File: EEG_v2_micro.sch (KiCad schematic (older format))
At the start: 0 parts

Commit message: Added CC2540 Bluetooth chip to library
Also added CC2540 to sch
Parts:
- added U6: CC2540, symbol CC2540
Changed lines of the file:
@@
 Sheet 2 4
 Title "Project Synapse Prototype Board"
-Date "12 jan 2015"
+Date "13 jan 2015"
 Rev "A.b"
 Comp "Senior Design 14-15"
@@
 Comment4 ""
 $EndDescr
+$Comp
+L CC2540 U6
+U 1 1 54B4D13C
+P 5450 4250
+F 0 "U6" H 5450 4150 60  0000 C CNN
+F 1 "CC2540" H 5450 4300 60  0000 C CNN
+F 2 "" H 5450 4300 60  0000 C CNN
+F 3 "" H 5450 4300 60  0000 C CNN
+	1    5450 4250
+	1    0    0    -1
+$EndComp
 $EndSCHEMATC

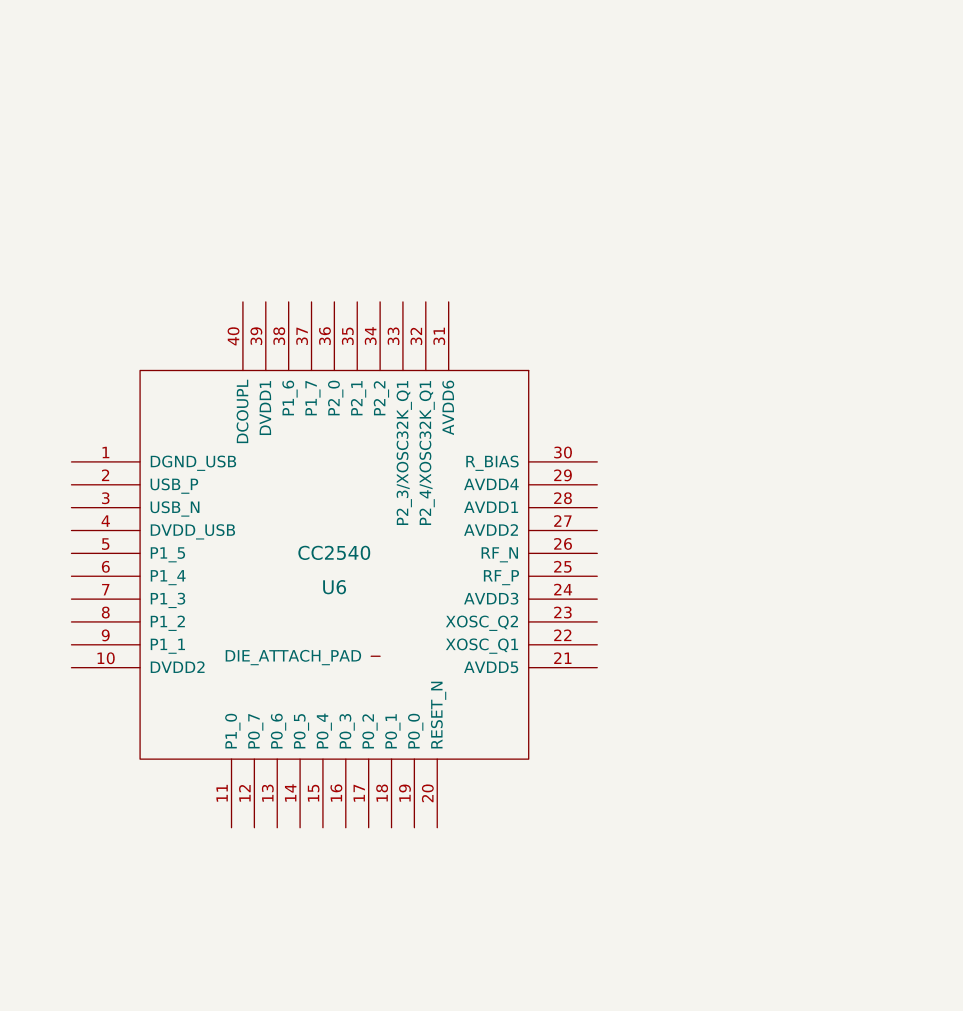
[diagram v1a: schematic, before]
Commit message: Finished CC2540 Symbol, Added example application schematic
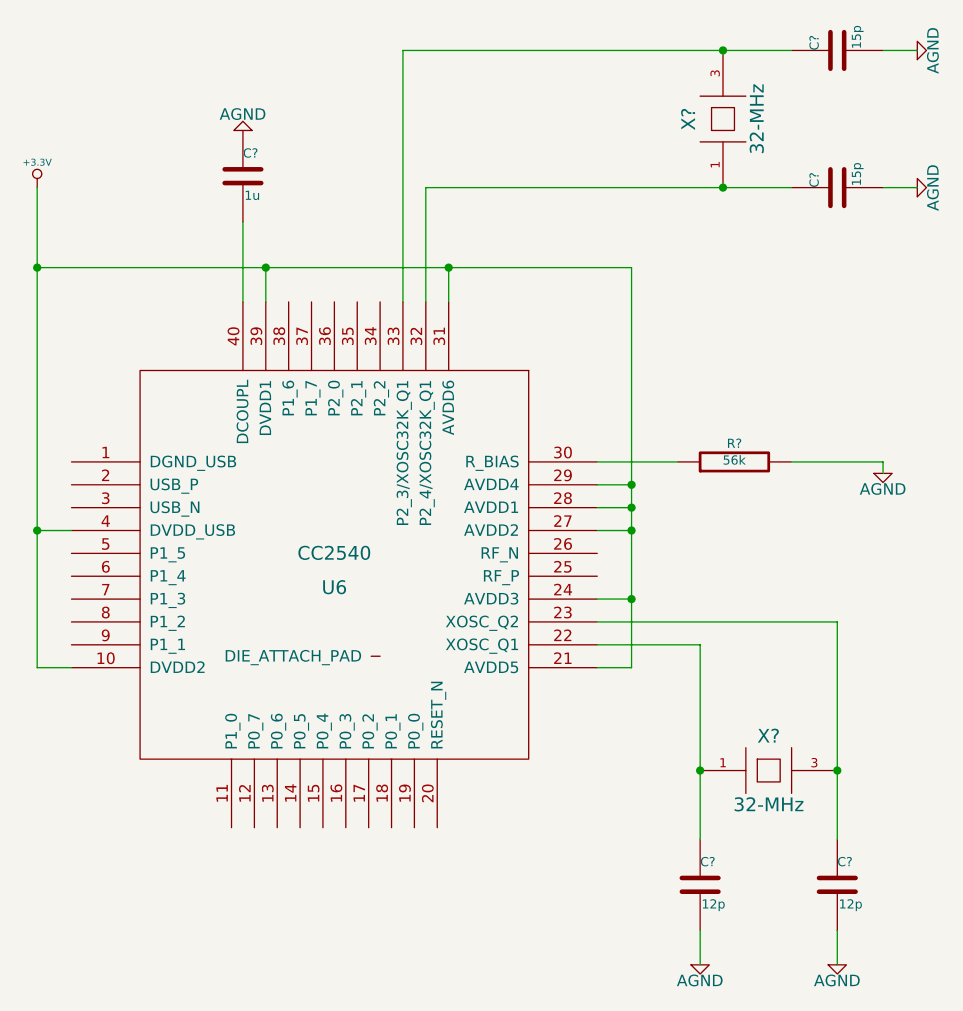
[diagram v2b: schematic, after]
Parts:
- added C?: 1u, ~, symbol C
- added C? (x2): 12p, ~, symbol C
- added C? (x2): 15p, ~, symbol C
- added R?: 56k, ~, symbol R
- added X? (x2): 32-MHz, ~, symbol QUARTZCMS4
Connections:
- net +3.3V: now reaches U6.10 (DVDD2)
- net +3.3V: now also U6.21 (AVDD5), U6.24 (AVDD3), U6.27 (AVDD2), U6.28 (AVDD1), U6.29 (AVDD4), U6.31 (AVDD6), U6.39 (DVDD1), U6.4 (DVDD_USB)
- net at U6.22 (XOSC_Q1): now also C?.1, X?.1
- net at U6.23 (XOSC_Q2): now also C?.1, X?.3
- net at U6.30 (R_BIAS): now also R?.1
- net at U6.32 (P2_4/XOSC32K_Q1): now also C?.1, X?.1
- net at U6.33 (P2_3/XOSC32K_Q1): now also C?.1, X?.3
- net at U6.40 (DCOUPL): now also C?.2
- new net AGND: C?.1, C?.2, C?.2, C?.2, C?.2, R?.2
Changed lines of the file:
@@
 	1    0    0    -1
 $EndComp
+$Comp
+L C C?
+U 1 1 54B4DAF5
+P 5050 2550
+F 0 "C?" H 5050 2650 40  0000 L CNN
+F 1 "1u" H 5056 2465 40  0000 L CNN
+F 2 "~" H 5088 2400 30  0000 C CNN
+F 3 "~" H 5050 2550 60  0000 C CNN
+	1    5050 2550
+	1    0    0    -1
+$EndComp
+Wire Wire Line
+	5050 2750 5050 3100
+$Comp
+L AGND #PWR?
+U 1 1 54B4DC2F
+P 5050 2350
+F 0 "#PWR?" H 5050 2350 40  0001 C CNN
+F 1 "AGND" H 5050 2280 50  0000 C CNN
+F 2 "~" H 5050 2350 60  0000 C CNN
+F 3 "~" H 5050 2350 60  0000 C CNN
+	1    5050 2350
+	-1   0    0    1
+$EndComp
+$Comp
+L R R?
+U 1 1 54B4DE9D
+P 7200 3800
+F 0 "R?" V 7280 3800 40  0000 C CNN
+F 1 "56k" V 7207 3801 40  0000 C CNN
+F 2 "~" V 7130 3800 30  0000 C CNN
+F 3 "~" H 7200 3800 30  0000 C CNN
+	1    7200 3800
+	0    -1   -1   0
+$EndComp
+Wire Wire Line
+	6950 3800 6600 3800
+Wire Wire Line
+	7450 3800 7850 3800
+$Comp
+L AGND #PWR?
+U 1 1 54B4DEBC
+P 7850 3850
+F 0 "#PWR?" H 7850 3850 40  0001 C CNN
+F 1 "AGND" H 7850 3780 50  0000 C CNN
+F 2 "~" H 7850 3850 60  0000 C CNN
+F 3 "~" H 7850 3850 60  0000 C CNN
+	1    7850 3850
+	1    0    0    -1
+$EndComp
+Wire Wire Line
+	7850 3800 7850 3850
+Wire Wire Line
+	6750 4700 6600 4700
+Wire Wire Line
+	6750 2950 6750 4700
+Wire Wire Line
+	6750 4400 6600 4400
+Wire Wire Line
+	6750 4100 6600 4100
+Connection ~ 6750 4400
+Wire Wire Line
+	6750 4000 6600 4000
+Connection ~ 6750 4100
+Wire Wire Line
+	6750 3900 6600 3900
+Connection ~ 6750 4000
+Wire Wire Line
+	4150 2950 6750 2950
+Wire Wire Line
+	5950 2950 5950 3100
+Connection ~ 6750 3900
+Wire Wire Line
+	5150 2950 5150 3100
+Connection ~ 5950 2950
+Wire Wire Line
+	4150 2600 4150 4700
+Wire Wire Line
+	4150 4100 4300 4100
+Connection ~ 5150 2950
+Wire Wire Line
+	4150 4700 4300 4700
+Connection ~ 4150 4100
+Connection ~ 4150 2950
+$Comp
+L +3.3V #PWR?
+U 1 1 54B4DF64
+P 4150 2600
+F 0 "#PWR?" H 4150 2560 30  0001 C CNN
+F 1 "+3.3V" H 4150 2710 30  0000 C CNN
+F 2 "~" H 4150 2600 60  0000 C CNN
+F 3 "~" H 4150 2600 60  0000 C CNN
+	1    4150 2600
+	1    0    0    -1
+$EndComp
+$Comp
+L QUARTZCMS4 X?
+U 1 1 54B4E091
+P 7350 5150
+F 0 "X?" H 7350 5300 60  0000 C CNN
+F 1 "32-MHz" H 7350 5000 60  0000 C CNN
+F 2 "~" H 7350 5150 60  0000 C CNN
+F 3 "~" H 7350 5150 60  0000 C CNN
+	1    7350 5150
+	1    0    0    -1
+$EndComp
+Wire Wire Line
+	7050 4600 7050 5450
+Wire Wire Line
+	7050 4600 6600 4600
+Wire Wire Line
+	6600 4500 7650 4500
+Wire Wire Line
+	7650 4500 7650 5450
+$Comp
+L C C?
+U 1 1 54B4E0D9
+P 7050 5650
+F 0 "C?" H 7050 5750 40  0000 L CNN
+F 1 "12p" H 7056 5565 40  0000 L CNN
+F 2 "~" H 7088 5500 30  0000 C CNN
+F 3 "~" H 7050 5650 60  0000 C CNN
+	1    7050 5650
+	1    0    0    -1
+$EndComp
+$Comp
+L C C?
+U 1 1 54B4E0DF
+P 7650 5650
+F 0 "C?" H 7650 5750 40  0000 L CNN
+F 1 "12p" H 7656 5565 40  0000 L CNN
+F 2 "~" H 7688 5500 30  0000 C CNN
+F 3 "~" H 7650 5650 60  0000 C CNN
+	1    7650 5650
+	1    0    0    -1
+$EndComp
+Connection ~ 7050 5150
+Connection ~ 7650 5150
+$Comp
+L AGND #PWR?
+U 1 1 54B4E155
+P 7050 6000
+F 0 "#PWR?" H 7050 6000 40  0001 C CNN
+F 1 "AGND" H 7050 5930 50  0000 C CNN
+F 2 "~" H 7050 6000 60  0000 C CNN
+F 3 "~" H 7050 6000 60  0000 C CNN
+	1    7050 6000
+	1    0    0    -1
+$EndComp
+$Comp
+L AGND #PWR?
+U 1 1 54B4E15B
+P 7650 6000
+F 0 "#PWR?" H 7650 6000 40  0001 C CNN
+F 1 "AGND" H 7650 5930 50  0000 C CNN
+F 2 "~" H 7650 6000 60  0000 C CNN
+F 3 "~" H 7650 6000 60  0000 C CNN
+	1    7650 6000
+	1    0    0    -1
+$EndComp
+Wire Wire Line
+	7650 5850 7650 6000
+Wire Wire Line
+	7050 5850 7050 6000
+$Comp
+L QUARTZCMS4 X?
+U 1 1 54B4E2E4
+P 7150 2300
+F 0 "X?" H 7150 2450 60  0000 C CNN
+F 1 "32-MHz" H 7150 2150 60  0000 C CNN
+F 2 "~" H 7150 2300 60  0000 C CNN
+F 3 "~" H 7150 2300 60  0000 C CNN
+	1    7150 2300
+	0    -1   -1   0
+$EndComp
+Wire Wire Line
+	5850 2600 7450 2600
+Wire Wire Line
+	5850 2600 5850 3100
+Wire Wire Line
+	5750 3100 5750 2000
+Wire Wire Line
+	5750 2000 7450 2000
+$Comp
+L C C?
+U 1 1 54B4E361
+P 7650 2600
+F 0 "C?" H 7650 2700 40  0000 L CNN
+F 1 "15p" H 7656 2515 40  0000 L CNN
+F 2 "~" H 7688 2450 30  0000 C CNN
+F 3 "~" H 7650 2600 60  0000 C CNN
+	1    7650 2600
+	0    -1   -1   0
+$EndComp
+$Comp
+L C C?
+U 1 1 54B4E367
+P 7650 2000
+F 0 "C?" H 7650 2100 40  0000 L CNN
+F 1 "15p" H 7656 1915 40  0000 L CNN
+F 2 "~" H 7688 1850 30  0000 C CNN
+F 3 "~" H 7650 2000 60  0000 C CNN
+	1    7650 2000
+	0    -1   -1   0
+$EndComp
+$Comp
+L AGND #PWR?
+U 1 1 54B4E36D
+P 8000 2600
+F 0 "#PWR?" H 8000 2600 40  0001 C CNN
+F 1 "AGND" H 8000 2530 50  0000 C CNN
+F 2 "~" H 8000 2600 60  0000 C CNN
+F 3 "~" H 8000 2600 60  0000 C CNN
+	1    8000 2600
+	0    -1   -1   0
+$EndComp
+$Comp
+L AGND #PWR?
+U 1 1 54B4E373
+P 8000 2000
+F 0 "#PWR?" H 8000 2000 40  0001 C CNN
+F 1 "AGND" H 8000 1930 50  0000 C CNN
+F 2 "~" H 8000 2000 60  0000 C CNN
+F 3 "~" H 8000 2000 60  0000 C CNN
+	1    8000 2000
+	0    -1   -1   0
+$EndComp
+Wire Wire Line
+	7850 2000 8000 2000
+Wire Wire Line
+	7850 2600 8000 2600
+Connection ~ 7150 2000
+Connection ~ 7150 2600
 $EndSCHEMATC

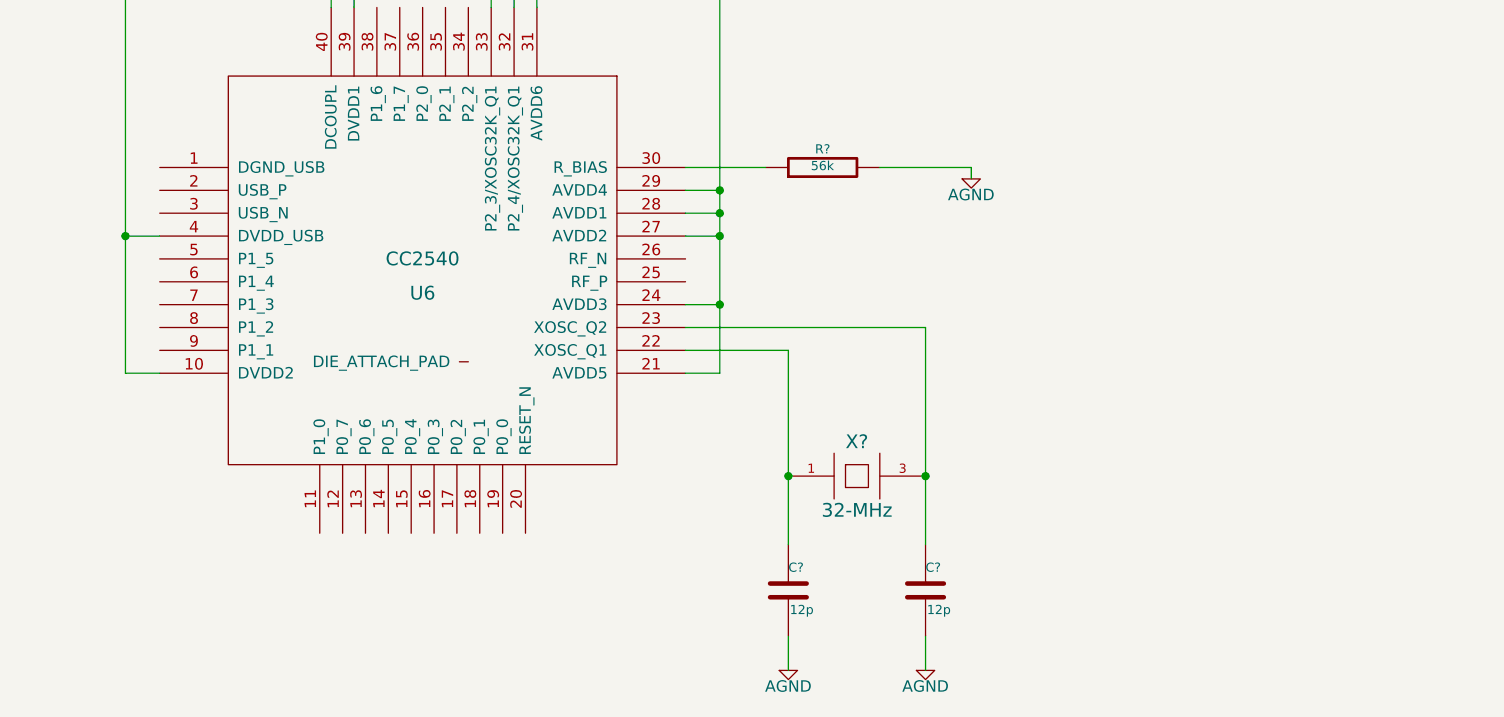
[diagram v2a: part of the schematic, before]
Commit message: Pin connect, add note on Balun and antenna
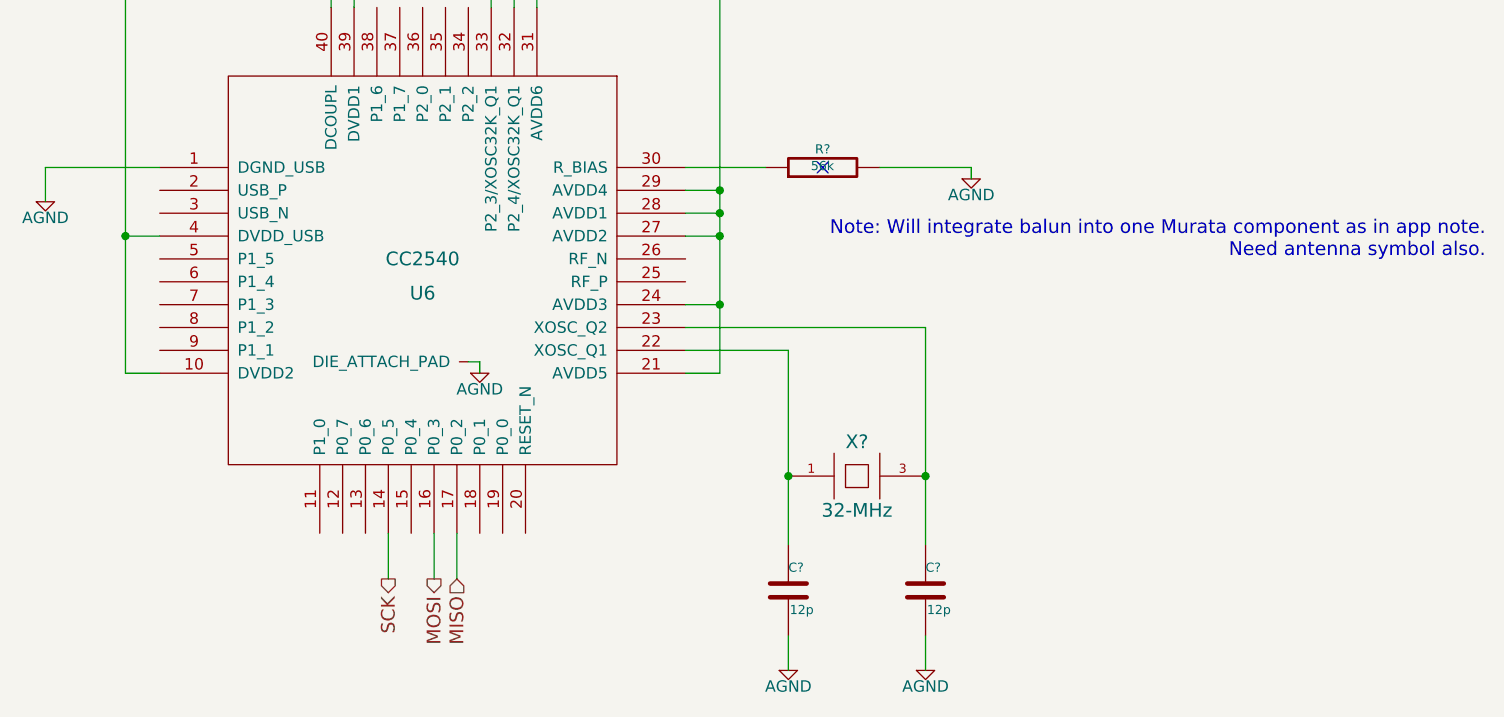
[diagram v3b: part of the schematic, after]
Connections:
- net AGND: now also U6.1 (DGND_USB), U6.~ (DIE_ATTACH_PAD)
- net SCK: now reaches U6.14 (P0_5)
- net MOSI: now reaches U6.16 (P0_3)
- net MISO: now reaches U6.17 (P0_2)
- no-connect marks 0 -> 1
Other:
- note added: "Note: Will integrate balun into one Murata component as in app note.\n Need antenna symbol also."
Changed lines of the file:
@@
 $Descr USLetter 11000 8500
 encoding utf-8
-Sheet 2 4
+Sheet 4 4
 Title "Project Synapse Prototype Board"
 Date "13 jan 2015"
@@
 Connection ~ 7150 2000
 Connection ~ 7150 2600
+$Comp
+L AGND #PWR?
+U 1 1 54B4E516
+P 5700 4700
+F 0 "#PWR?" H 5700 4700 40  0001 C CNN
+F 1 "AGND" H 5700 4630 50  0000 C CNN
+F 2 "~" H 5700 4700 60  0000 C CNN
+F 3 "~" H 5700 4700 60  0000 C CNN
+	1    5700 4700
+	1    0    0    -1
+$EndComp
+Wire Wire Line
+	5650 4650 5700 4650
+Wire Wire Line
+	5700 4650 5700 4700
+$Comp
+L AGND #PWR?
+U 1 1 54B4E69D
+P 3800 3950
+F 0 "#PWR?" H 3800 3950 40  0001 C CNN
+F 1 "AGND" H 3800 3880 50  0000 C CNN
+F 2 "~" H 3800 3950 60  0000 C CNN
+F 3 "~" H 3800 3950 60  0000 C CNN
+	1    3800 3950
+	1    0    0    -1
+$EndComp
+Wire Wire Line
+	4300 3800 3800 3800
+Wire Wire Line
+	3800 3800 3800 3950
+Text HLabel 5500 5600 3    60   Output ~ 0
+MOSI
+Text HLabel 5600 5600 3    60   Input ~ 0
+MISO
+Text HLabel 5300 5600 3    60   Output ~ 0
+SCK
+NoConn ~ 7200 3800
+Wire Wire Line
+	5300 5400 5300 5600
+Wire Wire Line
+	5500 5400 5500 5600
+Wire Wire Line
+	5600 5400 5600 5600
+Text Notes 10100 4200 2    60   ~ 0
+Note: Will integrate balun into one Murata component as in app note.\n Need antenna symbol also.
 $EndSCHEMATC
